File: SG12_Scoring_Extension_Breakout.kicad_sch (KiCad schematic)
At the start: 37 parts, among them J1 RJ45, J10 Conn_01x02, J11 Conn_01x02, J12 Conn_01x02, J13 Conn_01x02, J14 Conn_01x02, J15 Conn_01x02, J16 Conn_02x04_Top_Bottom, J17 Conn_02x04_Top_Bottom, J18 Conn_02x04_Top_Bottom, J19 Conn_01x02, J2 Barrel_Jack_MountingPin, J3 Barrel_Jack_MountingPin, J4 Barrel_Jack_MountingPin, J5 Barrel_Jack_MountingPin, J6 Barrel_Jack_MountingPin, J7 Barrel_Jack_MountingPin, J8 Conn_02x08_Odd_Even, J9 Barrel_Jack_MountingPin, Q1 IRF4905, Q2 IRF4905, Q3 IRF4905, Q4 IRF4905, Q5 IRF4905, Q6 IRF4905

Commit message: Flipped connections on mini-fit connectors to match EPS12V
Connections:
- net +12V: now also J18.5 (Pin_5), J18.6 (Pin_6), J18.7 (Pin_7), J18.8 (Pin_8); no longer J18.1 (Pin_1), J18.2 (Pin_2), J18.3 (Pin_3), J18.4 (Pin_4)
- net GND: now also J16.1 (Pin_1), J16.2 (Pin_2), J16.3 (Pin_3), J16.4 (Pin_4), J17.1 (Pin_1), J17.2 (Pin_2), J17.3 (Pin_3), J17.4 (Pin_4), J18.1 (Pin_1), J18.2 (Pin_2), J18.3 (Pin_3), J18.4 (Pin_4); no longer J16.5 (Pin_5), J16.6 (Pin_6), J16.7 (Pin_7), J16.8 (Pin_8), J17.5 (Pin_5), J17.6 (Pin_6), J17.7 (Pin_7), J17.8 (Pin_8), J18.5 (Pin_5), J18.6 (Pin_6), J18.7 (Pin_7), J18.8 (Pin_8)
- net Green_PullUp: now also J16.5 (Pin_5), J17.5 (Pin_5); no longer J16.1 (Pin_1), J17.1 (Pin_1)
- net Red_PullUp: now also J16.6 (Pin_6), J17.6 (Pin_6); no longer J16.2 (Pin_2), J17.2 (Pin_2)
- net WhiteG_PullUp: now also J16.7 (Pin_7), J17.7 (Pin_7); no longer J16.3 (Pin_3), J17.3 (Pin_3)
- net WhiteR_PullUp: now also J16.8 (Pin_8), J17.8 (Pin_8); no longer J16.4 (Pin_4), J17.4 (Pin_4)

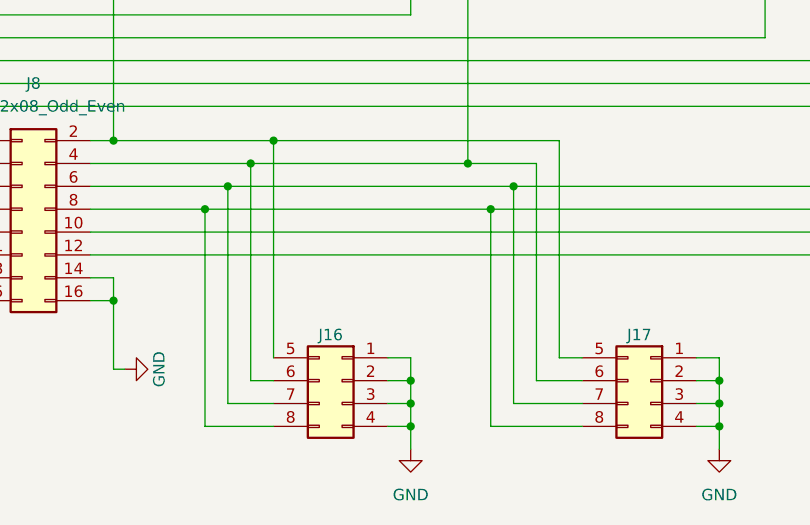
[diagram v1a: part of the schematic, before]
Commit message: Switched connections for easier routing later
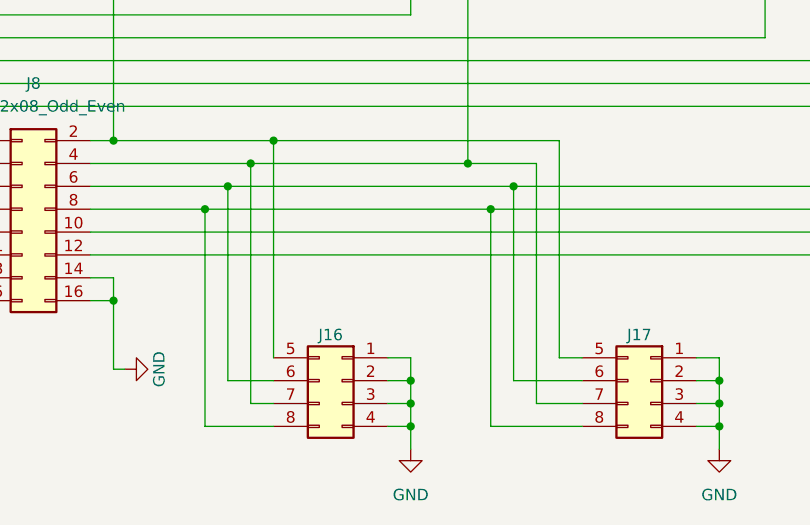
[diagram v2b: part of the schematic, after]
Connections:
- net Red_PullUp: now also J16.7 (Pin_7), J17.7 (Pin_7); no longer J16.6 (Pin_6), J17.6 (Pin_6)
- net WhiteG_PullUp: now also J16.6 (Pin_6), J17.6 (Pin_6); no longer J16.7 (Pin_7), J17.7 (Pin_7)
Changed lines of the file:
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@@
-    (stroke (width 0) (type default))
-  )
-  (wire (pts (xy 87.63 143.51) (xy 85.09 143.51))
     (stroke (width 0) (type default))
   )
@@
     (stroke (width 0) (type default))
   )
+  (wire (pts (xy 116.84 146.05) (xy 121.92 146.05))
+    (stroke (width 0) (type default))
+  )
   (wire (pts (xy 69.85 132.08) (xy 69.85 134.62))
     (stroke (width 0) (type default))
@@
     (stroke (width 0) (type default))
   )
+  (wire (pts (xy 85.09 146.05) (xy 87.63 146.05))
+    (stroke (width 0) (type default))
+  )
   (wire (pts (xy 50.8 110.49) (xy 219.71 110.49))
     (stroke (width 0) (type default))
@@
     (stroke (width 0) (type default))
   )
+  (wire (pts (xy 82.55 143.51) (xy 87.63 143.51))
+    (stroke (width 0) (type default))
+  )
   (wire (pts (xy 193.04 67.31) (xy 194.31 67.31))
     (stroke (width 0) (type default))
@@
     (stroke (width 0) (type default))
   )
-  (wire (pts (xy 114.3 146.05) (xy 121.92 146.05))
-    (stroke (width 0) (type default))
-  )
   (wire (pts (xy 271.78 74.93) (xy 271.78 71.12))
     (stroke (width 0) (type default))
@@
     (stroke (width 0) (type default))
   )
-  (wire (pts (xy 116.84 119.38) (xy 116.84 143.51))
+  (wire (pts (xy 116.84 119.38) (xy 116.84 146.05))
     (stroke (width 0) (type default))
   )
@@
     (stroke (width 0) (type default))
   )
-  (wire (pts (xy 85.09 143.51) (xy 85.09 119.38))
+  (wire (pts (xy 85.09 119.38) (xy 85.09 146.05))
     (stroke (width 0) (type default))
   )
@@
     (stroke (width 0) (type default))
   )
-  (wire (pts (xy 82.55 146.05) (xy 87.63 146.05))
-    (stroke (width 0) (type default))
-  )
   (wire (pts (xy 114.3 67.31) (xy 115.57 67.31))
     (stroke (width 0) (type default))
@@
     (stroke (width 0) (type default))
   )
-  (wire (pts (xy 116.84 143.51) (xy 121.92 143.51))
-    (stroke (width 0) (type default))
-  )
   (wire (pts (xy 102.87 146.05) (xy 102.87 148.59))
     (stroke (width 0) (type default))
@@
     (stroke (width 0) (type default))
   )
+  (wire (pts (xy 114.3 143.51) (xy 121.92 143.51))
+    (stroke (width 0) (type default))
+  )
   (wire (pts (xy 100.33 140.97) (xy 102.87 140.97))
     (stroke (width 0) (type default))
@@
     (stroke (width 0) (type default))
   )
-  (wire (pts (xy 82.55 121.92) (xy 82.55 146.05))
+  (wire (pts (xy 82.55 121.92) (xy 82.55 143.51))
     (stroke (width 0) (type default))
   )
@@
     (stroke (width 0) (type default))
   )
-  (wire (pts (xy 114.3 121.92) (xy 114.3 146.05))
-    (stroke (width 0) (type default))
-  )
+  (wire (pts (xy 114.3 121.92) (xy 114.3 143.51))
+    (stroke (width 0) (type default))
+  )

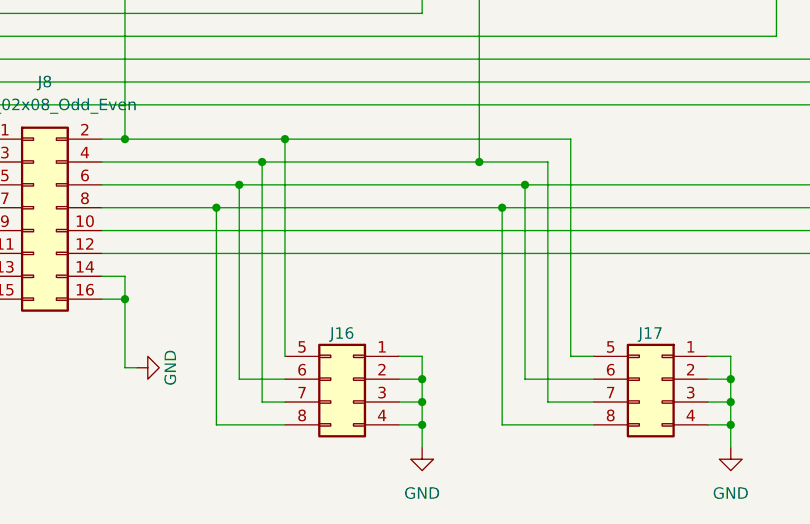
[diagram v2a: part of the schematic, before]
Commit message: Switched more connections for easier routing later
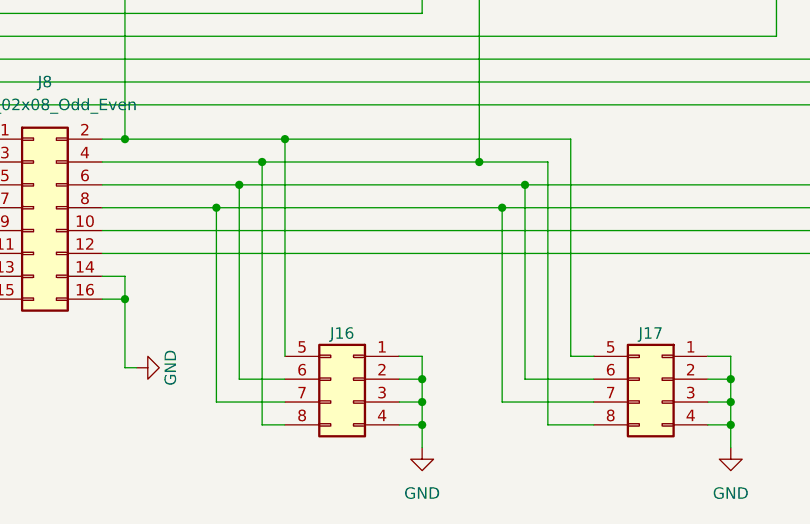
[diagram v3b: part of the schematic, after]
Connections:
- net Red_PullUp: now also J16.8 (Pin_8), J17.8 (Pin_8); no longer J16.7 (Pin_7), J17.7 (Pin_7)
- net WhiteR_PullUp: now also J16.7 (Pin_7), J17.7 (Pin_7); no longer J16.8 (Pin_8), J17.8 (Pin_8)
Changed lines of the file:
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@@
+    (stroke (width 0) (type default))
+  )
+  (wire (pts (xy 111.76 146.05) (xy 121.92 146.05))
     (stroke (width 0) (type default))
   )
@@
     (stroke (width 0) (type default))
   )
-  (wire (pts (xy 80.01 124.46) (xy 80.01 148.59))
-    (stroke (width 0) (type default))
-  )
   (wire (pts (xy 92.71 77.47) (xy 93.98 77.47))
     (stroke (width 0) (type default))
@@
     (stroke (width 0) (type default))
   )
-  (wire (pts (xy 116.84 146.05) (xy 121.92 146.05))
+  (wire (pts (xy 111.76 146.05) (xy 111.76 124.46))
     (stroke (width 0) (type default))
   )
@@
     (stroke (width 0) (type default))
   )
+  (wire (pts (xy 80.01 124.46) (xy 80.01 146.05))
+    (stroke (width 0) (type default))
+  )
   (wire (pts (xy 48.26 107.95) (xy 48.26 124.46))
     (stroke (width 0) (type default))
@@
     (stroke (width 0) (type default))
   )
-  (wire (pts (xy 111.76 148.59) (xy 111.76 124.46))
-    (stroke (width 0) (type default))
-  )
   (wire (pts (xy 231.14 67.31) (xy 232.41 67.31))
     (stroke (width 0) (type default))
@@
     (stroke (width 0) (type default))
   )
+  (wire (pts (xy 80.01 146.05) (xy 87.63 146.05))
+    (stroke (width 0) (type default))
+  )
   (wire (pts (xy 193.04 74.93) (xy 193.04 73.66))
     (stroke (width 0) (type default))
@@
     (stroke (width 0) (type default))
   )
-  (wire (pts (xy 85.09 146.05) (xy 87.63 146.05))
-    (stroke (width 0) (type default))
-  )
   (wire (pts (xy 50.8 110.49) (xy 219.71 110.49))
     (stroke (width 0) (type default))
@@
     (stroke (width 0) (type default))
   )
-  (wire (pts (xy 116.84 119.38) (xy 116.84 146.05))
+  (wire (pts (xy 116.84 119.38) (xy 116.84 148.59))
     (stroke (width 0) (type default))
   )
@@
     (stroke (width 0) (type default))
   )
-  (wire (pts (xy 85.09 119.38) (xy 85.09 146.05))
+  (wire (pts (xy 85.09 119.38) (xy 85.09 148.59))
     (stroke (width 0) (type default))
   )
@@
     (stroke (width 0) (type default))
   )
-  (wire (pts (xy 80.01 148.59) (xy 87.63 148.59))
-    (stroke (width 0) (type default))
-  )
   (wire (pts (xy 148.59 67.31) (xy 148.59 73.66))
     (stroke (width 0) (type default))
@@
     (stroke (width 0) (type default))
   )
+  (wire (pts (xy 85.09 148.59) (xy 87.63 148.59))
+    (stroke (width 0) (type default))
+  )
   (wire (pts (xy 212.09 67.31) (xy 214.63 67.31))
     (stroke (width 0) (type default))
@@
     (stroke (width 0) (type default))
   )
-  (wire (pts (xy 111.76 148.59) (xy 121.92 148.59))
-    (stroke (width 0) (type default))
-  )
   (wire (pts (xy 247.65 77.47) (xy 247.65 67.31))
     (stroke (width 0) (type default))
@@
     (stroke (width 0) (type default))
   )
+  (wire (pts (xy 121.92 148.59) (xy 116.84 148.59))
+    (stroke (width 0) (type default))
+  )

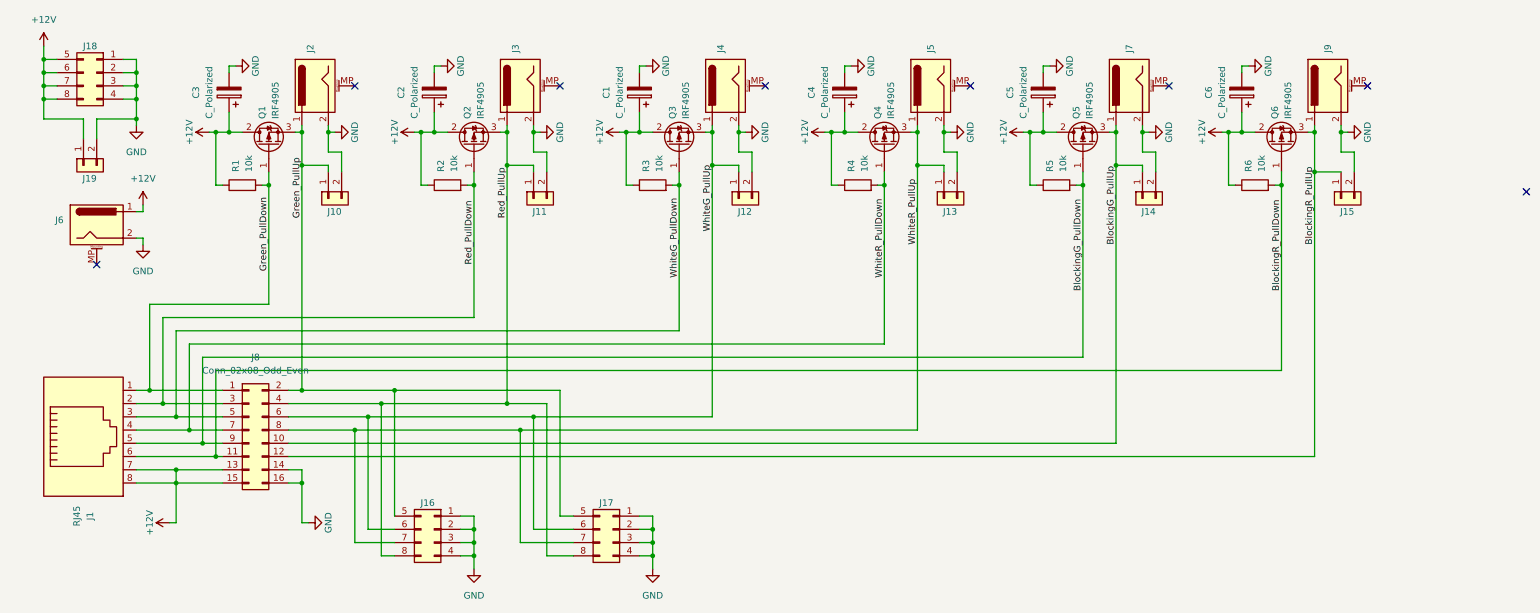
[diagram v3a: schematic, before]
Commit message: Schematic Symbol Names
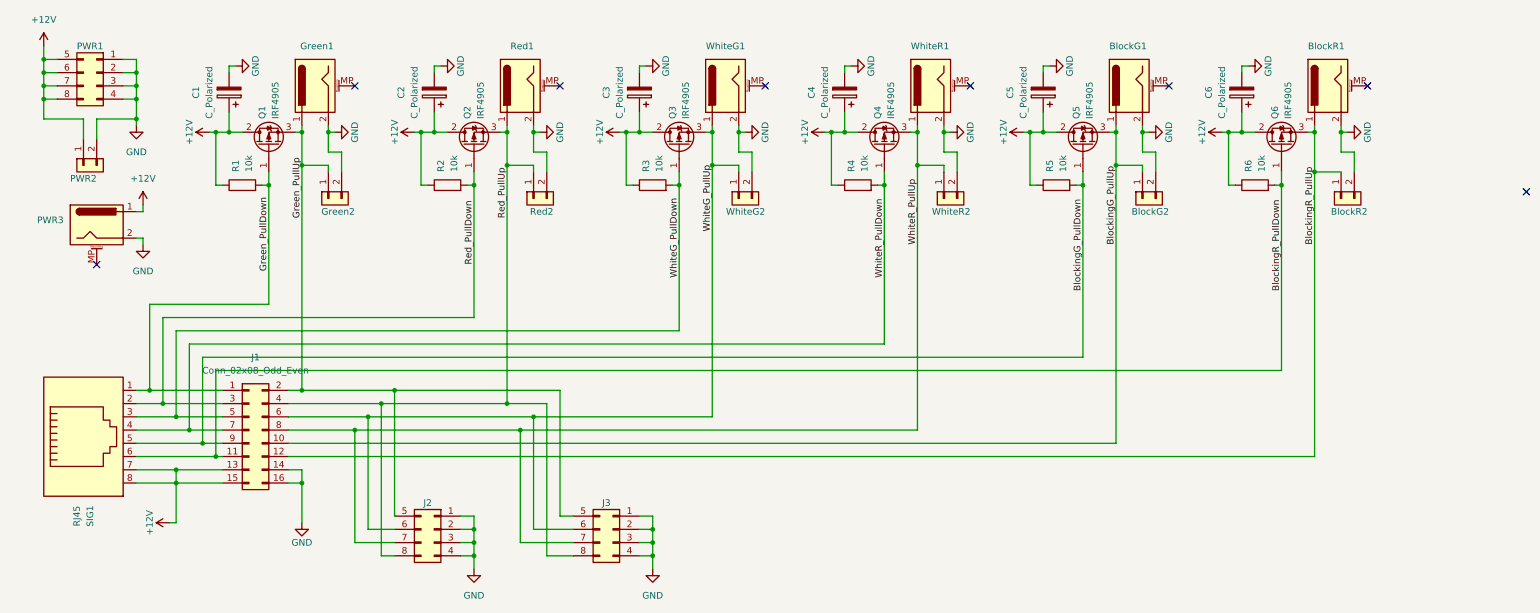
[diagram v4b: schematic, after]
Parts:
- renumbered J7 to BlockG1, J14 to BlockG2, J9 to BlockR1, J15 to BlockR2, C3 to C1, C1 to C3, J2 to Green1, J10 to Green2, J8 to J1, J16 to J2, J17 to J3, J18 to PWR1, J19 to PWR2, J6 to PWR3, J3 to Red1, J11 to Red2, J1 to SIG1, J4 to WhiteG1, J12 to WhiteG2, J5 to WhiteR1, J13 to WhiteR2

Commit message: Power flags for ERC checker
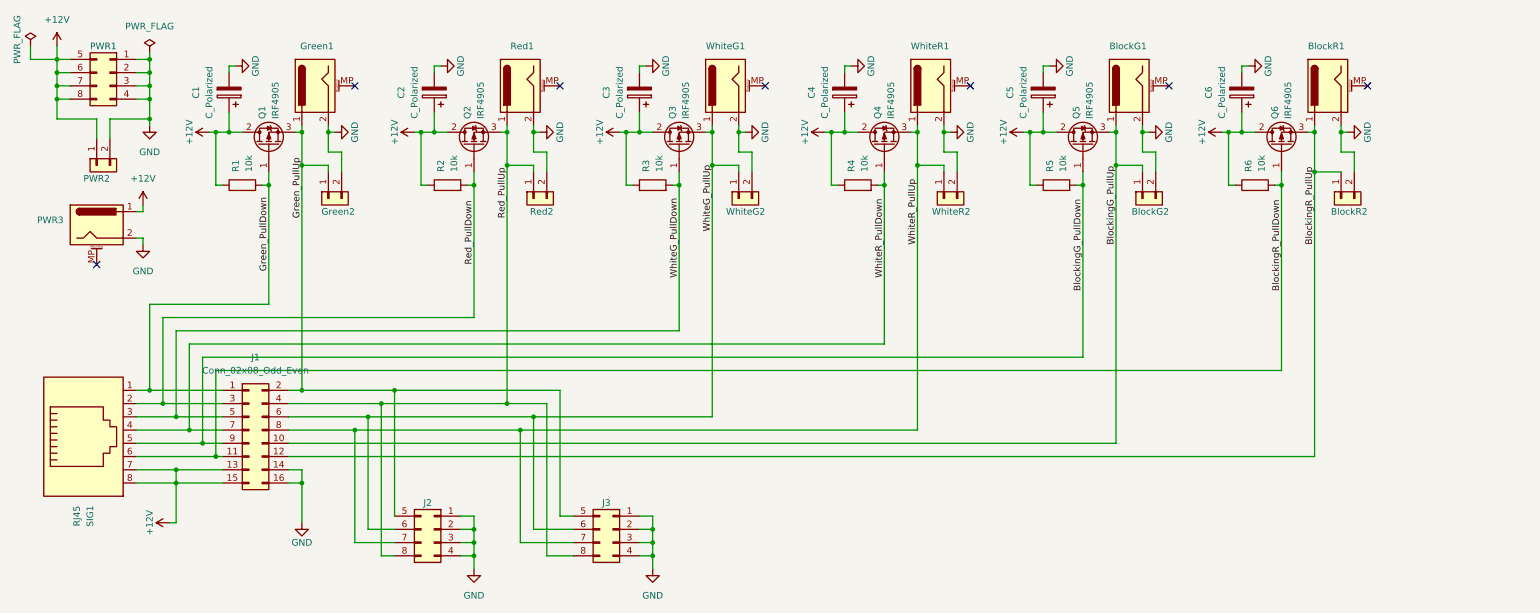
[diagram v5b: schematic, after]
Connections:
- no-connect marks 8 -> 7
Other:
- moved on the sheet: PWR1, PWR2

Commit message: Footprint modifications
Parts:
- BlockG2, BlockR2, Green2, PWR2, Red2, WhiteG2, WhiteR2: footprint Connector_Phoenix_MSTB:PhoenixContact_MSTBA_2,5_2-G-5,08_1x02_P5.08mm_Horizontal -> Library:PhoenixContact_MSTBA_2,5_2-G-5,08_1x02_P5.08mm_Horizontal
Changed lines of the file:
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@@
       (effects (font (size 1.27 1.27)) (justify left) hide)
     )
-    (property "Footprint" "Connector_Phoenix_MSTB:PhoenixContact_MSTBA_2,5_2-G-5,08_1x02_P5.08mm_Horizontal" (at 269.24 80.01 0)
+    (property "Footprint" "Library:PhoenixContact_MSTBA_2,5_2-G-5,08_1x02_P5.08mm_Horizontal" (at 269.24 80.01 0)
       (effects (font (size 1.27 1.27)) hide)
     )
@@
       (effects (font (size 1.27 1.27)) (justify left) hide)
     )
-    (property "Footprint" "Connector_Phoenix_MSTB:PhoenixContact_MSTBA_2,5_2-G-5,08_1x02_P5.08mm_Horizontal" (at 231.14 80.01 0)
+    (property "Footprint" "Library:PhoenixContact_MSTBA_2,5_2-G-5,08_1x02_P5.08mm_Horizontal" (at 231.14 80.01 0)
       (effects (font (size 1.27 1.27)) hide)
     )
@@
       (effects (font (size 1.27 1.27)) (justify left) hide)
     )
-    (property "Footprint" "Connector_Phoenix_MSTB:PhoenixContact_MSTBA_2,5_2-G-5,08_1x02_P5.08mm_Horizontal" (at 114.3 80.01 0)
+    (property "Footprint" "Library:PhoenixContact_MSTBA_2,5_2-G-5,08_1x02_P5.08mm_Horizontal" (at 114.3 80.01 0)
       (effects (font (size 1.27 1.27)) hide)
     )
@@
       (effects (font (size 1.27 1.27)) (justify left) hide)
     )
-    (property "Footprint" "Connector_Phoenix_MSTB:PhoenixContact_MSTBA_2,5_2-G-5,08_1x02_P5.08mm_Horizontal" (at 30.48 73.66 0)
+    (property "Footprint" "Library:PhoenixContact_MSTBA_2,5_2-G-5,08_1x02_P5.08mm_Horizontal" (at 30.48 73.66 0)
       (effects (font (size 1.27 1.27)) hide)
     )
@@
       (effects (font (size 1.27 1.27)) (justify left) hide)
     )
-    (property "Footprint" "Connector_Phoenix_MSTB:PhoenixContact_MSTBA_2,5_2-G-5,08_1x02_P5.08mm_Horizontal" (at 153.67 80.01 0)
+    (property "Footprint" "Library:PhoenixContact_MSTBA_2,5_2-G-5,08_1x02_P5.08mm_Horizontal" (at 153.67 80.01 0)
       (effects (font (size 1.27 1.27)) hide)
     )
@@
       (effects (font (size 1.27 1.27)) (justify left) hide)
     )
-    (property "Footprint" "Connector_Phoenix_MSTB:PhoenixContact_MSTBA_2,5_2-G-5,08_1x02_P5.08mm_Horizontal" (at 74.93 80.01 0)
+    (property "Footprint" "Library:PhoenixContact_MSTBA_2,5_2-G-5,08_1x02_P5.08mm_Horizontal" (at 74.93 80.01 0)
       (effects (font (size 1.27 1.27)) hide)
     )
@@
       (effects (font (size 1.27 1.27)) (justify left) hide)
     )
-    (property "Footprint" "Connector_Phoenix_MSTB:PhoenixContact_MSTBA_2,5_2-G-5,08_1x02_P5.08mm_Horizontal" (at 193.04 80.01 0)
-      (effects (font (size 1.27 1.27)) hide)
-    )
+    (property "Footprint" "Library:PhoenixContact_MSTBA_2,5_2-G-5,08_1x02_P5.08mm_Horizontal" (at 193.04 80.01 0)
+      (effects (font (size 1.27 1.27)) hide)
+    )

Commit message: first manufactured board
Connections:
- net +12V: now also Q1.3 (S), Q2.3 (S), Q3.3 (S), Q4.3 (S), Q5.3 (S), Q6.3 (S); no longer Q1.2 (D), Q2.2 (D), Q3.2 (D), Q4.2 (D), Q5.2 (D), Q6.2 (D)
- net BlockingG_PullDown: now also Q3.1 (G); no longer Q5.1 (G)
- net BlockingG_PullUp: now also Q3.2 (D); no longer Q5.3 (S)
- net BlockingR_PullDown: now also Q2.1 (G); no longer Q6.1 (G)
- net BlockingR_PullUp: now also Q2.2 (D); no longer Q6.3 (S)
- net Green_PullUp: now also Q1.2 (D); no longer Q1.3 (S)
- net Red_PullDown: now also Q6.1 (G); no longer Q2.1 (G)
- net Red_PullUp: now also Q6.2 (D); no longer Q2.3 (S)
- net WhiteG_PullDown: now also Q5.1 (G); no longer Q3.1 (G)
- net WhiteG_PullUp: now also Q5.2 (D); no longer Q3.3 (S)
- net WhiteR_PullUp: now also Q4.2 (D); no longer Q4.3 (S)
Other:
- moved on the sheet: Q1, Q2, Q3, Q4, Q5, Q6
